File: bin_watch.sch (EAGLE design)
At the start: 106 parts, among them IC1 MEGA48/88/168-MU, J1 USB3100-XX-X_REVB, Q1 32.768kHz, T1 2N7002BKV, T2 2N7002BKV, T3 2N7002BKV, T4 2N7002BKV, T5 PMDT670UPE, T6 PMDT670UPE, T7 PMDT670UPE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

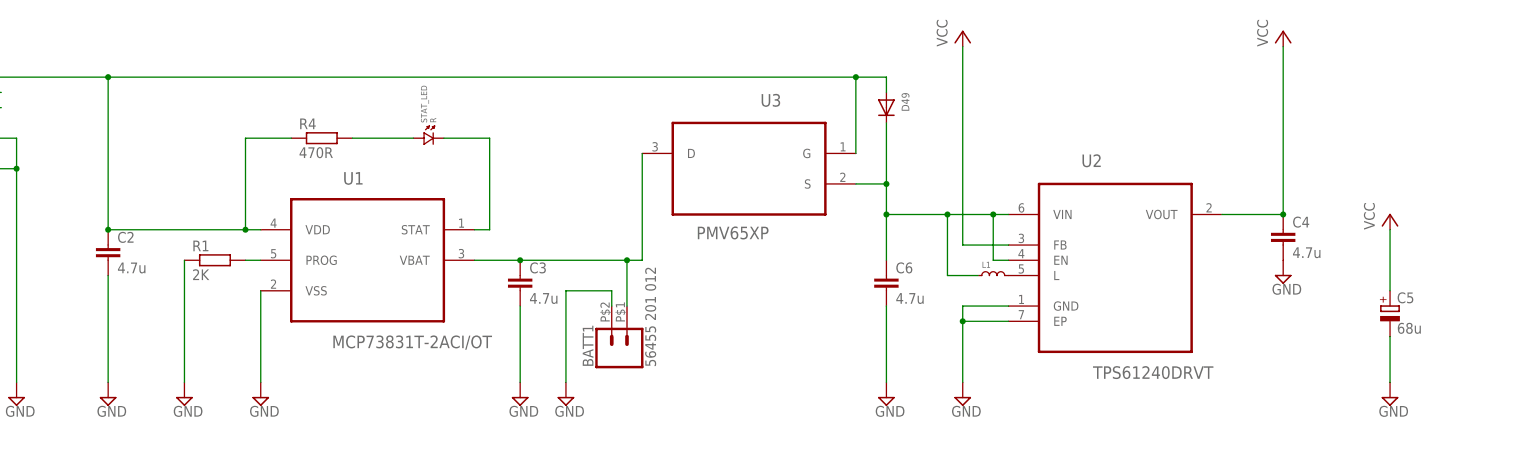
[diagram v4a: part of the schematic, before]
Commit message: Mass commit
This is a mess...
Added a new firmware attempt, this time in C language.
Several changes to the board
A a pull resistor for the gate of the power transistor
Stuff I forgot...
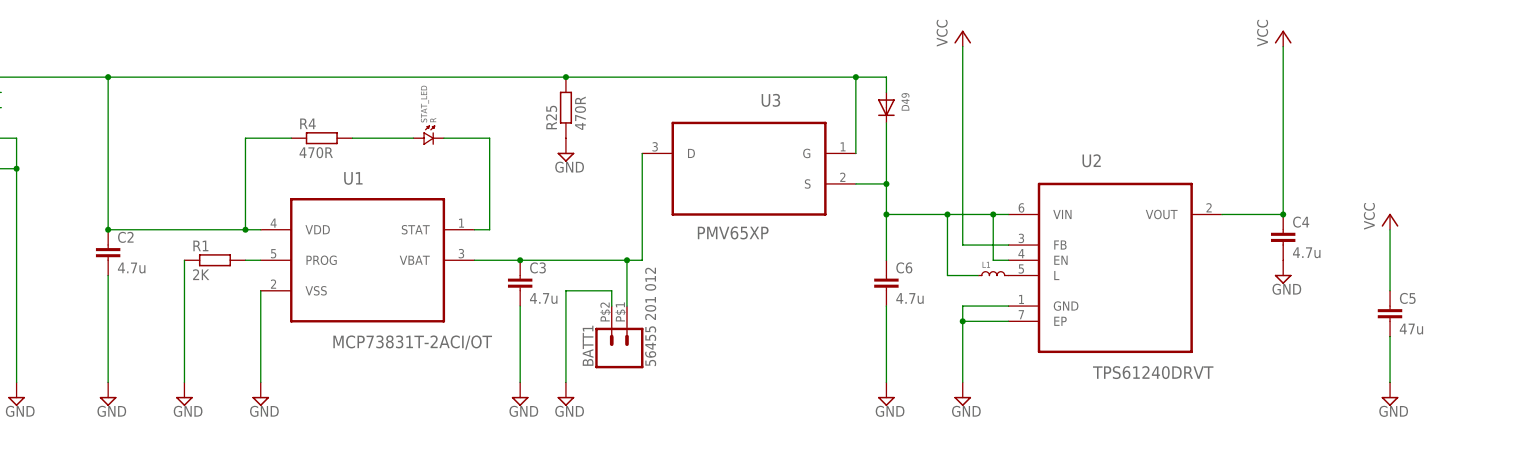
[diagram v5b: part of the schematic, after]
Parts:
- added R25: 470R, rcl:R-EU_R0603
- C5: value 68u -> 47u; device rcl:CPOL-EUB/3528-21R -> rcl:C-EUC0603
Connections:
- net GND: now also C5.2, R25.1; no longer C5.-
- net VBUS: now also R25.2
- net VCC: now also C5.1; no longer C5.+
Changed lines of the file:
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@@
 <part name="J1" library="USB3100-XX-X_REVB" deviceset="USB3100-XX-X_REVB" device=""/>
 <part name="P+9" library="supply1" library_urn="urn:adsk.eagle:library:371" deviceset="VCC" device=""/>
-<part name="C5" library="rcl" library_urn="urn:adsk.eagle:library:334" deviceset="CPOL-EU" device="B/3528-21R" package3d_urn="urn:adsk.eagle:package:23409/1" value="68u"/>
 <part name="R5" library="rcl" library_urn="urn:adsk.eagle:library:334" deviceset="R-EU_" device="R0603" package3d_urn="urn:adsk.eagle:package:23555/1" value="68"/>
 <part name="R6" library="rcl" library_urn="urn:adsk.eagle:library:334" deviceset="R-EU_" device="R0603" package3d_urn="urn:adsk.eagle:package:23555/1" value="68"/>
@@
 <part name="PAD13" library="wirepad" library_urn="urn:adsk.eagle:library:412" deviceset="SMD2" device="" package3d_urn="urn:adsk.eagle:package:30839/1"/>
 <part name="PAD14" library="wirepad" library_urn="urn:adsk.eagle:library:412" deviceset="SMD2" device="" package3d_urn="urn:adsk.eagle:package:30839/1"/>
+<part name="C5" library="rcl" library_urn="urn:adsk.eagle:library:334" deviceset="C-EU" device="C0603" package3d_urn="urn:adsk.eagle:package:23616/2" value="47u"/>
+<part name="R25" library="rcl" library_urn="urn:adsk.eagle:library:334" deviceset="R-EU_" device="R0603" package3d_urn="urn:adsk.eagle:package:23555/1" value="470R"/>
+<part name="SUPPLY32" library="supply2" library_urn="urn:adsk.eagle:library:372" deviceset="GND" device=""/>
 </parts>
 <sheets>
@@
 <instance part="J1" gate="G$1" x="50.8" y="269.24" rot="MR0"/>
 <instance part="P+9" gate="VCC" x="299.72" y="254"/>
-<instance part="C5" gate="G$1" x="299.72" y="238.76"/>
 <instance part="R5" gate="G$1" x="266.7" y="71.12"/>
 <instance part="R6" gate="G$1" x="274.32" y="68.58"/>
@@
 <instance part="PAD13" gate="1" x="276.86" y="99.06" rot="R270"/>
 <instance part="PAD14" gate="1" x="279.4" y="99.06" rot="R270"/>
+<instance part="C5" gate="G$1" x="299.72" y="238.76"/>
+<instance part="R25" gate="G$1" x="162.56" y="271.78" rot="R90"/>
+<instance part="SUPPLY32" gate="GND" x="162.56" y="264.16"/>
 </instances>
 <busses>
@@
 <segment>
 <pinref part="SUPPLY15" gate="GND" pin="GND"/>
-<pinref part="C5" gate="G$1" pin="-"/>
 <wire x1="299.72" y1="226.06" x2="299.72" y2="233.68" width="0.1524" layer="91"/>
+<pinref part="C5" gate="G$1" pin="2"/>
 </segment>
 <segment>
@@
 <pinref part="R18" gate="G$1" pin="1"/>
 <pinref part="SUPPLY31" gate="GND" pin="GND"/>
+</segment>
+<segment>
+<pinref part="R25" gate="G$1" pin="1"/>
+<pinref part="SUPPLY32" gate="GND" pin="GND"/>
 </segment>
 </net>
@@
 <segment>
 <pinref part="P+9" gate="VCC" pin="VCC"/>
-<pinref part="C5" gate="G$1" pin="+"/>
 <wire x1="299.72" y1="251.46" x2="299.72" y2="241.3" width="0.1524" layer="91"/>
+<pinref part="C5" gate="G$1" pin="1"/>
 </segment>
 <segment>
@@
 <pinref part="J1" gate="G$1" pin="VBUS"/>
 <pinref part="U3" gate="A" pin="G"/>
-<wire x1="86.36" y1="276.86" x2="210.82" y2="276.86" width="0.1524" layer="91"/>
+<wire x1="86.36" y1="276.86" x2="162.56" y2="276.86" width="0.1524" layer="91"/>
+<wire x1="162.56" y1="276.86" x2="210.82" y2="276.86" width="0.1524" layer="91"/>
 <wire x1="210.82" y1="276.86" x2="210.82" y2="264.16" width="0.1524" layer="91"/>
 <pinref part="D49" gate="G$1" pin="A"/>
@@
 <junction x="86.36" y="276.86"/>
 <pinref part="R4" gate="G$1" pin="1"/>
+<pinref part="R25" gate="G$1" pin="2"/>
+<junction x="162.56" y="276.86"/>
 </segment>
 </net>
@@
 </sheet>
 </sheets>
-<errors>
-</errors>
 </schematic>
 </drawing>

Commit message: Everything fully routed
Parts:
- R25: value 470R -> 1M
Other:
- moved on the sheet: L1
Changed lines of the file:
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@@
 <part name="PAD14" library="wirepad" library_urn="urn:adsk.eagle:library:412" deviceset="SMD2" device="" package3d_urn="urn:adsk.eagle:package:30839/1"/>
 <part name="C5" library="rcl" library_urn="urn:adsk.eagle:library:334" deviceset="C-EU" device="C0603" package3d_urn="urn:adsk.eagle:package:23616/2" value="47u"/>
-<part name="R25" library="rcl" library_urn="urn:adsk.eagle:library:334" deviceset="R-EU_" device="R0603" package3d_urn="urn:adsk.eagle:package:23555/1" value="470R"/>
+<part name="R25" library="rcl" library_urn="urn:adsk.eagle:library:334" deviceset="R-EU_" device="R0603" package3d_urn="urn:adsk.eagle:package:23555/1" value="1M"/>
 <part name="SUPPLY32" library="supply2" library_urn="urn:adsk.eagle:library:372" deviceset="GND" device=""/>
 </parts>
@@
 <instance part="SUPPLY23" gate="GND" x="281.94" y="243.84"/>
 <instance part="C6" gate="G$1" x="215.9" y="243.84"/>
-<instance part="L1" gate="G$1" x="233.68" y="243.84"/>
+<instance part="L1" gate="G$1" x="231.14" y="243.84"/>
 <instance part="SUPPLY24" gate="GND" x="215.9" y="223.52"/>
 <instance part="U3" gate="A" x="193.04" y="264.16" rot="MR0"/>
@@
 <pinref part="L1" gate="G$1" pin="1"/>
 <wire x1="226.06" y1="254" x2="233.68" y2="254" width="0.1524" layer="91"/>
-<wire x1="231.14" y1="243.84" x2="226.06" y2="243.84" width="0.1524" layer="91"/>
+<wire x1="228.6" y1="243.84" x2="226.06" y2="243.84" width="0.1524" layer="91"/>
 <wire x1="226.06" y1="243.84" x2="226.06" y2="254" width="0.1524" layer="91"/>
 <junction x="226.06" y="254"/>
@@
 <pinref part="U2" gate="A" pin="L"/>
 <pinref part="L1" gate="G$1" pin="2"/>
-</segment>
-</net>
+<wire x1="233.68" y1="243.84" x2="236.22" y2="243.84" width="0.1524" layer="91"/>
+</segment>
+</net>

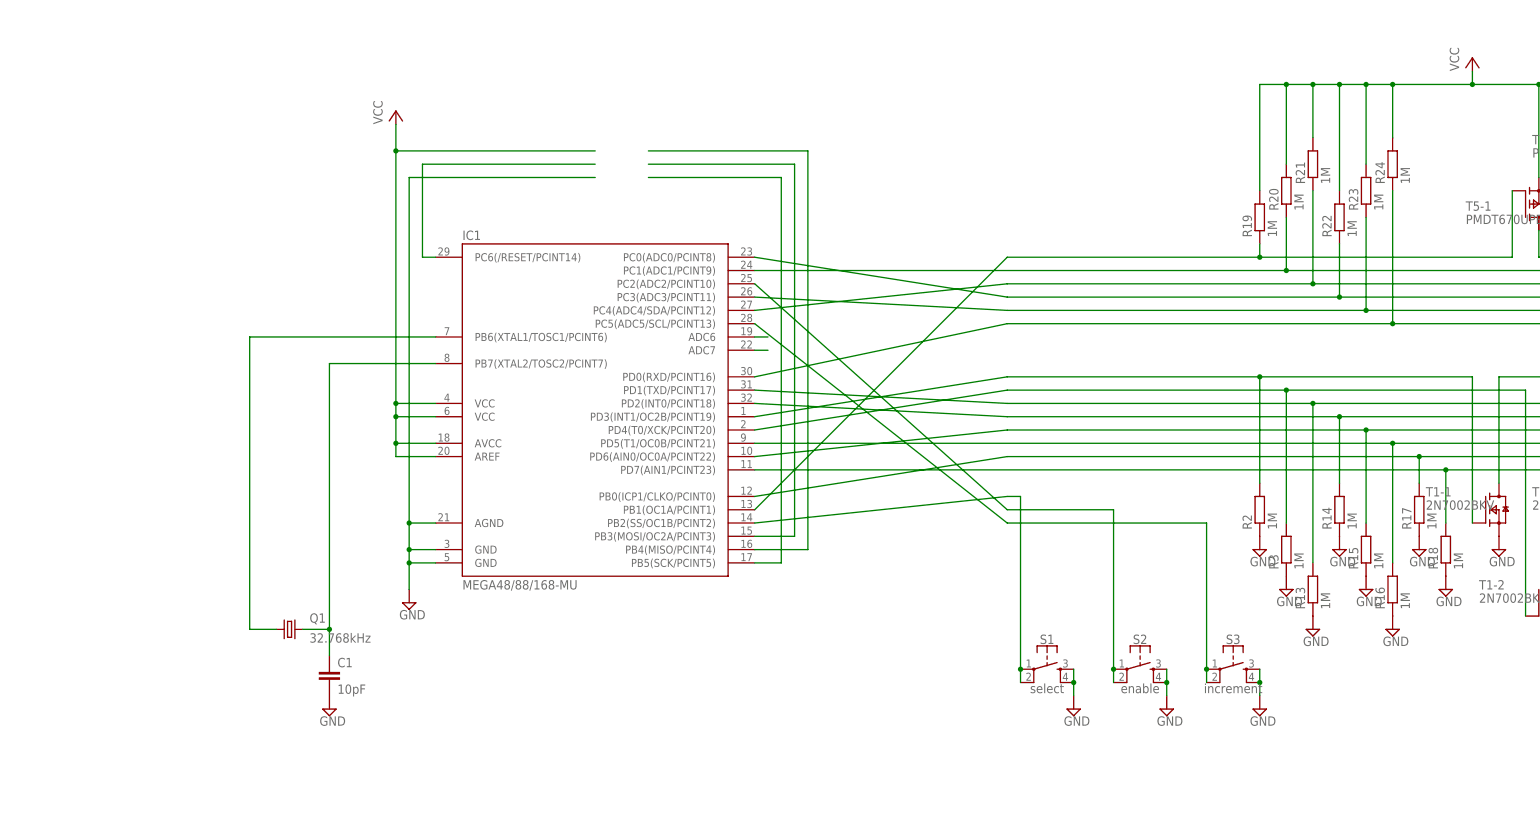
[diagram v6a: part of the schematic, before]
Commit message: Removed QFN32, placed QFN28
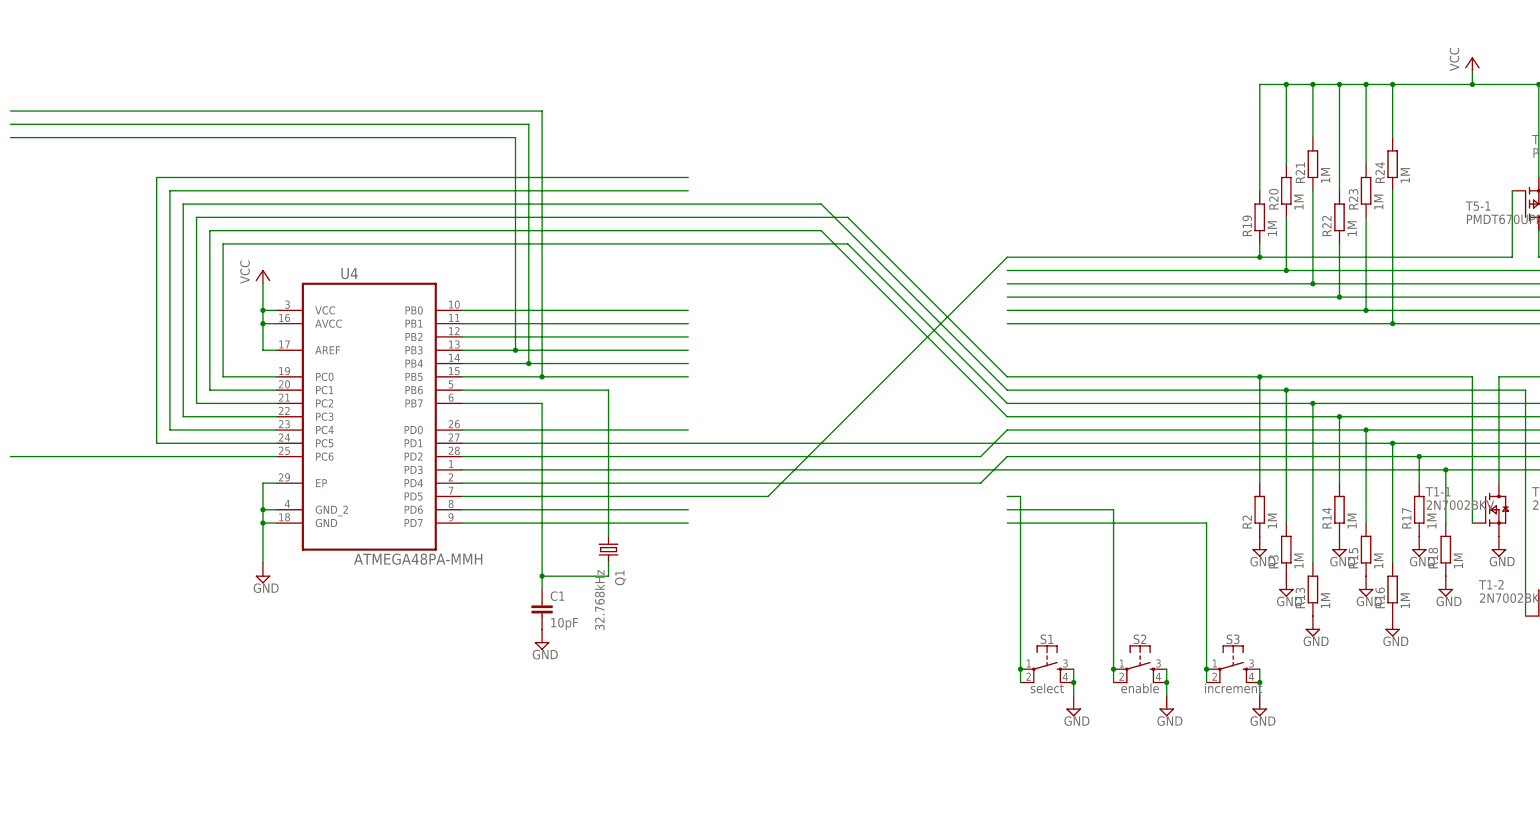
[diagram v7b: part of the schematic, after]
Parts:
- removed IC1: MEGA48/88/168-MU, avr-5:MEGA48/88/168-MU
- added U4: ATMEGA48PA-MMH, Atmel_By_element14_Batch_1-00:ATMEGA48PA-MMH
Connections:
- removed net ADC6: IC1.ADC6
- removed net ADC7: IC1.ADC7
- removed net MISO: IC1.PB4(MISO/PCINT4)
- removed net MOSI: IC1.PB3(MOSI/OC2A/PCINT3)
- removed net RST: IC1.PC6(/RESET/PCINT14)
- removed net SCK: IC1.PB5(SCK/PCINT5)
- new net N$10: U4.PC4
- new net N$11: U4.PC5
- new net N$12: U4.PB0
- new net N$13: U4.PB1
- new net N$14: U4.PB2
- new net N$15: U4.PD0
- new net N$2: U4.PB3
- new net N$21: U4.PD6
- new net N$22: U4.PD7
- new net N$3: U4.PC6
- new net N$4: U4.PB4
- new net N$5: U4.PB5
- net BTN1: no longer IC1.PB2(SS/OC1B/PCINT2)
- net BTN2: no longer IC1.PC2(ADC2/PCINT10)
- net BTN3: no longer IC1.PC5(ADC5/SCL/PCINT13)
- net GND: now also U4.EP, U4.GND, U4.GND_2; no longer IC1.AGND, IC1.GND@1, IC1.GND@2
- net G_BLOCK0: now also U4.PD5; no longer IC1.PB1(OC1A/PCINT1)
- net G_BLOCK1: no longer IC1.PC1(ADC1/PCINT9)
- net G_BLOCK2: no longer IC1.PC4(ADC4/SDA/PCINT12)
- net G_BLOCK3: no longer IC1.PC0(ADC0/PCINT8)
- net G_BLOCK4: no longer IC1.PC3(ADC3/PCINT11)
- net G_BLOCK5: no longer IC1.PD0(RXD/PCINT16)
- net G_LIGHT0: now also U4.PC2; no longer IC1.PD3(INT1/OC2B/PCINT19)
- net G_LIGHT1: now also U4.PC3; no longer IC1.PD4(T0/XCK/PCINT20)
- net G_LIGHT2: now also U4.PC0; no longer IC1.PD1(TXD/PCINT17)
- net G_LIGHT3: now also U4.PC1; no longer IC1.PD2(INT0/PCINT18)
- net G_LIGHT4: now also U4.PD2; no longer IC1.PD6(AIN0/OC0A/PCINT22)
- net G_LIGHT5: now also U4.PD1; no longer IC1.PD5(T1/OC0B/PCINT21)
- net G_LIGHT6: now also U4.PD4; no longer IC1.PB0(ICP1/CLKO/PCINT0)
- net G_LIGHT7: now also U4.PD3; no longer IC1.PD7(AIN1/PCINT23)
- net VCC: now also U4.AREF, U4.AVCC, U4.VCC; no longer IC1.AREF, IC1.AVCC, IC1.VCC@1, IC1.VCC@2
- net XTAL_N: now also U4.PB7; no longer IC1.PB7(XTAL2/TOSC2/PCINT7)
- net XTAL_P: now also U4.PB6; no longer IC1.PB6(XTAL1/TOSC1/PCINT6)
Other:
- moved on the sheet: C1, Q1
